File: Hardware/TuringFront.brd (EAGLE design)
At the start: 107 x 49.5 mm, 73 parts, among them T1 2N3904, U1 TL074_

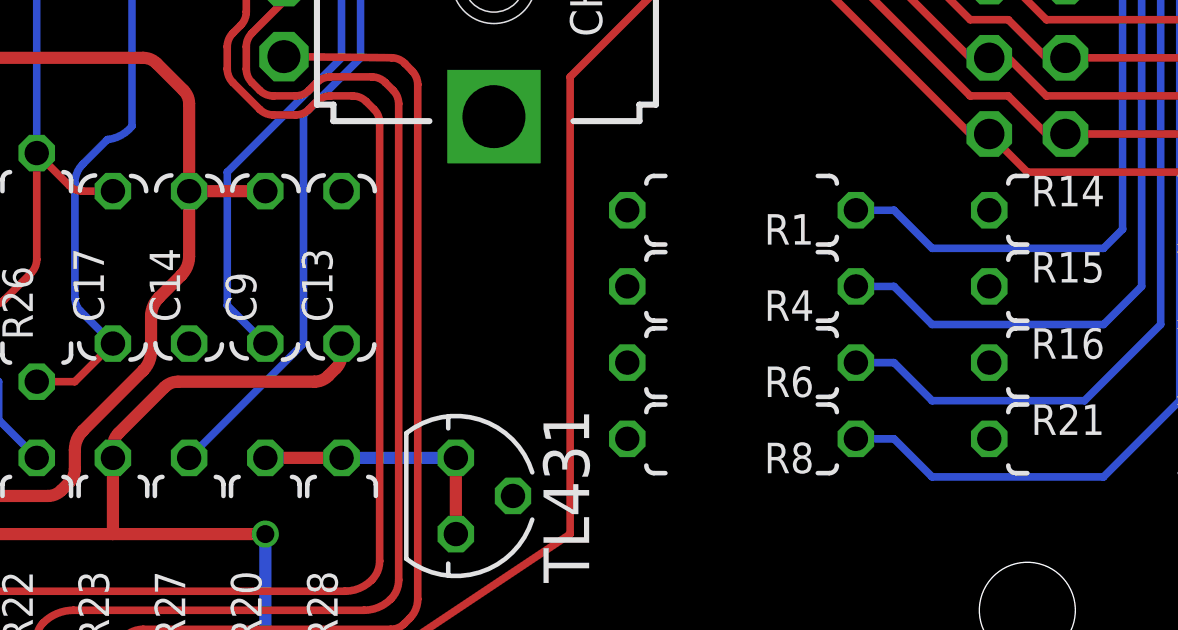
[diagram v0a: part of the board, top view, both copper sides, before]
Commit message: Increased spacing around ground planes
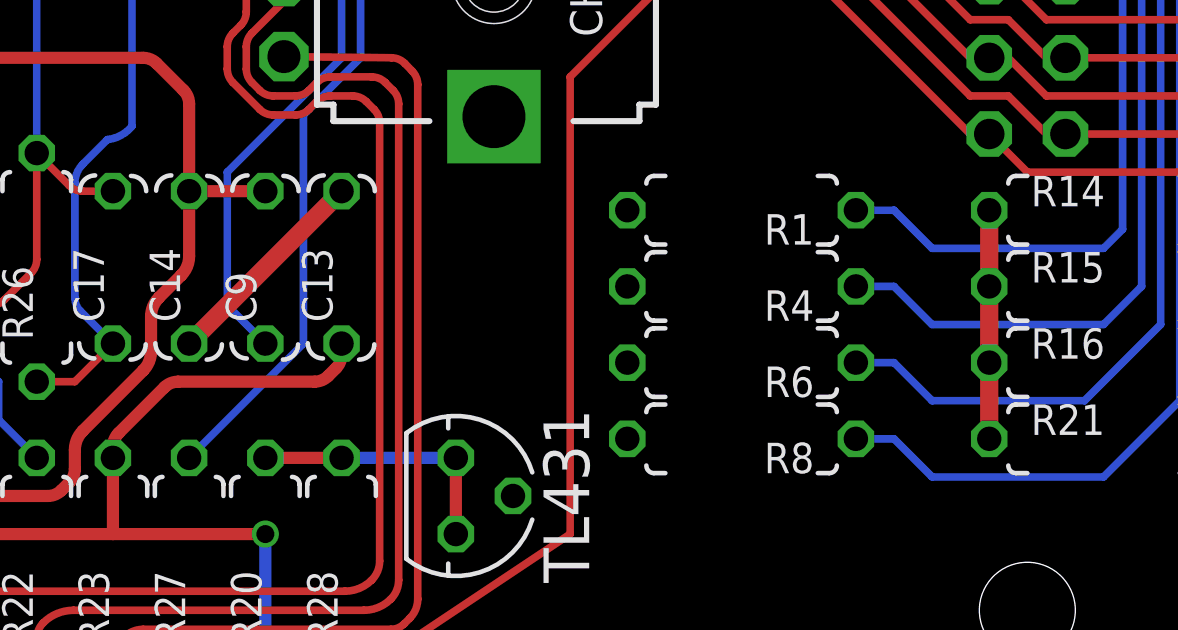
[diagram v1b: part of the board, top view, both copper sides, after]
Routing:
- net GND_FRONT: track 0.00 -> 14.8 mm
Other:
- board text added: "Music Thing Modular Turing Machine Rev 5 Front Board August 2017 CC-BY-SA"
- board text removed: "Music Thing Modular Turing Machine Rev 4 Front Board February 2016 CC-BY-SA"
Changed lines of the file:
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@@
 <?xml version="1.0" encoding="utf-8"?>
 <!DOCTYPE eagle SYSTEM "eagle.dtd">
-<eagle version="7.4.0">
+<eagle version="7.7.0">
 <drawing>
 <settings>
@@
 <layer number="19" name="Unrouted" color="6" fill="1" visible="no" active="yes"/>
 <layer number="20" name="Dimension" color="15" fill="1" visible="no" active="yes"/>
-<layer number="21" name="tPlace" color="7" fill="1" visible="yes" active="yes"/>
-<layer number="22" name="bPlace" color="7" fill="1" visible="no" active="yes"/>
-<layer number="23" name="tOrigins" color="15" fill="1" visible="yes" active="yes"/>
-<layer number="24" name="bOrigins" color="15" fill="1" visible="no" active="yes"/>
-<layer number="25" name="tNames" color="7" fill="1" visible="yes" active="yes"/>
-<layer number="26" name="bNames" color="7" fill="1" visible="no" active="yes"/>
-<layer number="27" name="tValues" color="7" fill="1" visible="yes" active="yes"/>
-<layer number="28" name="bValues" color="7" fill="1" visible="no" active="yes"/>
+<layer number="21" name="tPlace" color="7" fill="1" visible="no" active="yes"/>
+<layer number="22" name="bPlace" color="7" fill="1" visible="yes" active="yes"/>
+<layer number="23" name="tOrigins" color="15" fill="1" visible="no" active="yes"/>
+<layer number="24" name="bOrigins" color="15" fill="1" visible="yes" active="yes"/>
+<layer number="25" name="tNames" color="7" fill="1" visible="no" active="yes"/>
+<layer number="26" name="bNames" color="7" fill="1" visible="yes" active="yes"/>
+<layer number="27" name="tValues" color="7" fill="1" visible="no" active="yes"/>
+<layer number="28" name="bValues" color="7" fill="1" visible="yes" active="yes"/>
 <layer number="29" name="tStop" color="7" fill="3" visible="no" active="yes"/>
 <layer number="30" name="bStop" color="7" fill="6" visible="no" active="yes"/>
@@
 <wire x1="-15.875" y1="24.75" x2="121.285" y2="24.75" width="0.05" layer="51"/>
 <text x="81.28" y="38.1" size="1.27" layer="22" font="vector" ratio="12" distance="40" rot="MR270" align="top-left">Music Thing Modular Turing Machine
-Rev 4 Front Board
-February 2016 CC-BY-SA
+Rev 5 Front Board
+August 2017 CC-BY-SA
 </text>
 <wire x1="85.725" y1="36.83" x2="84.455" y2="36.83" width="0.4064" layer="51"/>
@@
 <signal name="N$2">
 <contactref element="CLOCK" pad="P$1_TIP"/>
-<contactref element="CLOCK" pad="P$1_TIP"/>
 <contactref element="R2" pad="1"/>
 <wire x1="1.35" y1="43.815" x2="1.35" y2="38.2522625" width="0.254" layer="1"/>
@@
 <contactref element="R16" pad="1"/>
 <contactref element="R21" pad="1"/>
-<polygon width="0.8128" layer="16">
+<polygon width="0.8128" layer="16" isolate="0.4064">
 <vertex x="0" y="50.8"/>
 <vertex x="107.95" y="50.8"/>
@@
 </polygon>
 <contactref element="U1" pad="3"/>
+<wire x1="66.675" y1="38.735" x2="61.595" y2="38.735" width="0" layer="19" extent="1-1"/>
+<wire x1="67.31" y1="12.7" x2="72.39" y2="17.78" width="0.6096" layer="1"/>
+<wire x1="93.98" y1="17.145" x2="93.98" y2="14.605" width="0.6096" layer="1"/>
+<wire x1="93.98" y1="14.605" x2="93.98" y2="12.065" width="0.6096" layer="1"/>
+<wire x1="93.98" y1="12.065" x2="93.98" y2="9.525" width="0.6096" layer="1"/>
 </signal>
 <signal name="WRITE_SW_FRONT">
